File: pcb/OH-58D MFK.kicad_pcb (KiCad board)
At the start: 2 copper layers, 114.5 x 140 mm, 123 parts, among them J1 Conn_01x07_Pin, J2 Conn_01x10_Pin, J3 Conn_01x03_Pin, J4 Conn_01x02_Pin, J5 Conn_01x02_Pin, SW1 SW_Push, SW10 SW_Push, SW11 SW_Push, SW12 SW_Push, SW13 SW_Push, SW14 SW_Push, SW15 SW_Push, SW16 SW_Push, SW17 SW_Push, SW18 SW_Push, SW19 SW_Push, SW2 SW_Push, SW20 SW_Push, SW21 SW_Push, SW22 SW_Push, SW23 SW_Push, SW24 SW_Push, SW25 SW_Push, SW26 SW_Push, SW27 SW_Push, SW28 SW_Push, SW29 SW_Push, SW3 SW_Push, SW30 SW_Push, SW31 SW_Push, SW32 SW_Push, SW33 SW_Push, SW34 SW_Push, SW35 SW_Push, SW36 SW_Push, SW37 SW_Push, SW38 SW_Push, SW39 SW_Push, SW4 SW_Push, SW40 SW_Push, SW41 SW_Push, SW42 SW_Push, SW43 SW_Push, SW44 SW_Push, SW45 SW_Push, SW46 SW_Push, SW47 SW_Push, SW5 SW_Push, SW6 SW_Push, SW7 SW_Push, SW8 SW_Push, SW9 SW_Push

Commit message: Change version prefix
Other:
- board text added: "${TITLE} v${REVISION}"
- board text removed: "${TITLE} r${REVISION}"
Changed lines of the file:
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@@
 		)
 	)
-	(gr_text "${TITLE} r${REVISION}"
+	(gr_text "${TITLE} v${REVISION}"
 		(at 111.825 113.725 0)
 		(layer "F.SilkS")

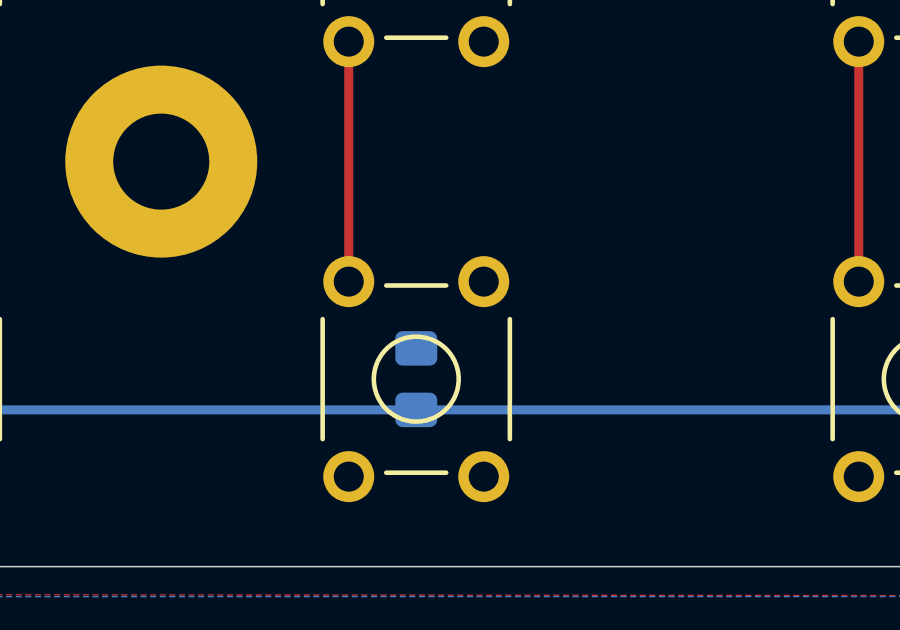
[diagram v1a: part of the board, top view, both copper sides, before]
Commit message: Add missing trace for D44 (#2)
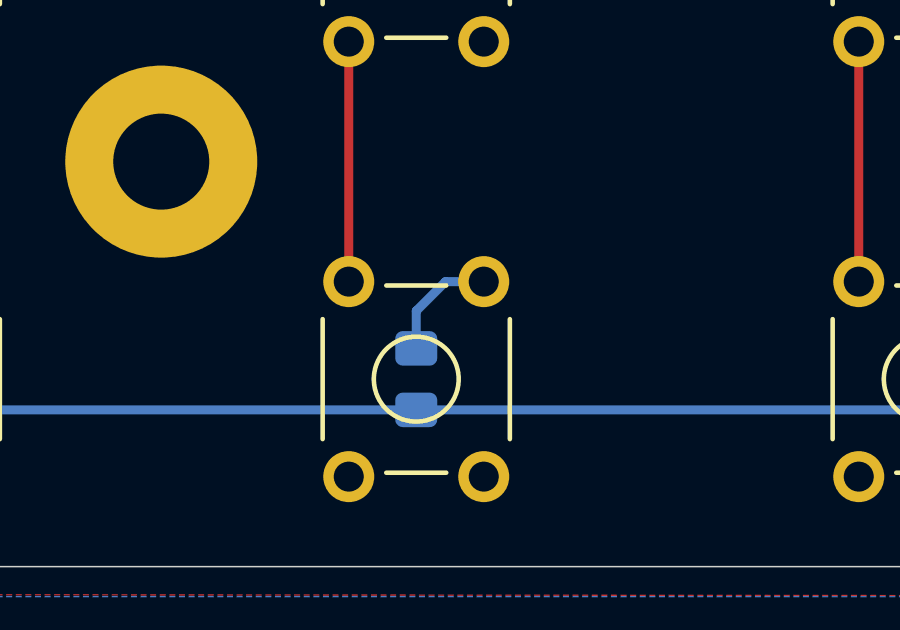
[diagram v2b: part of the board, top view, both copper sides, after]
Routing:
- net Net-(D44-A): track 0.00 -> 3.90 mm
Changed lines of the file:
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@@
+	)
+	(segment
+		(start 94.9 166.25)
+		(end 95.875 165.275)
+		(width 0.3)
+		(layer "B.Cu")
+		(net 53)
+	)
+	(segment
+		(start 94.9 167.5)
+		(end 94.9 166.25)
+		(width 0.3)
+		(layer "B.Cu")
+		(net 53)
+	)
+	(segment
+		(start 95.875 165.275)
+		(end 97.15 165.275)
+		(width 0.3)
+		(layer "B.Cu")
+		(net 53)
 	)
 	(segment
